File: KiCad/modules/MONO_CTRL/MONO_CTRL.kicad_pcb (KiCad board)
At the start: 4 copper layers, 15 x 14.8 mm, 50 parts, among them J1 Conn_01x01_Pin, J11 Conn_01x01_Pin, J12 Conn_01x01_Pin, J13 Conn_01x01_Pin, J14 Conn_01x01_Pin, J15 Conn_01x01_Pin, J16 Conn_01x01_Pin, J17 Conn_01x01_Pin, J18 Conn_01x01_Pin, J19 Conn_01x01_Pin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

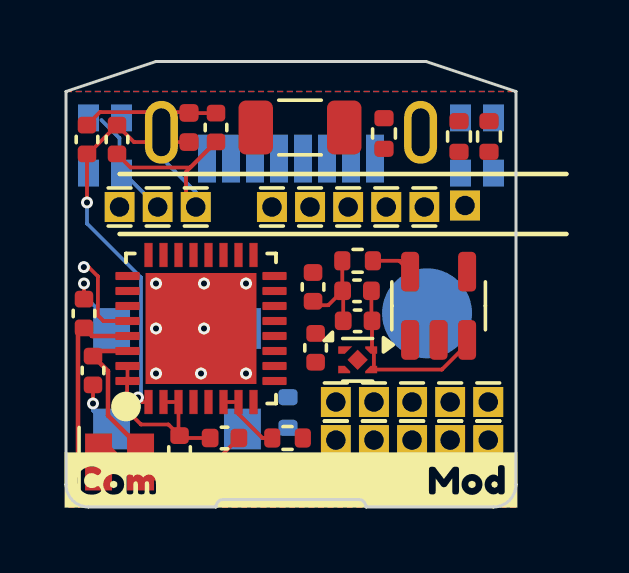
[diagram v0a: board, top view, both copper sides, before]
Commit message: finished mono moudule, should be ready for manufacture
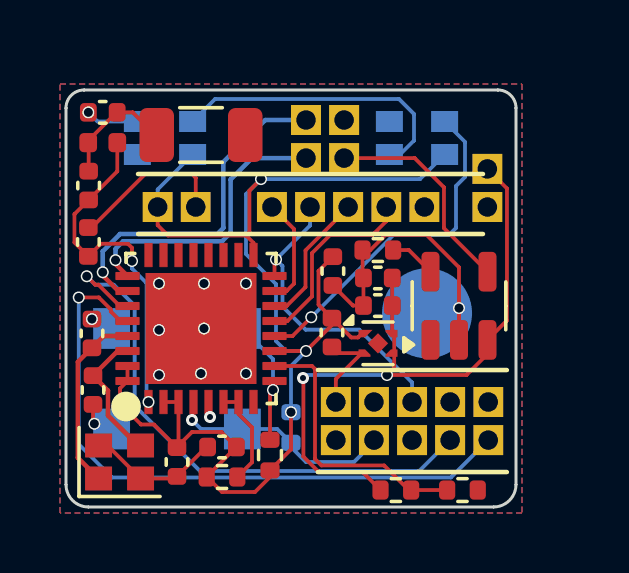
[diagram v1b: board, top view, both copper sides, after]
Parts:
- removed J19: Conn_01x01_Pin, Connector_PinHeader_1.27mm:PinHeader_1x01_P1.27mm_Vertical
- removed USB1: YTC-TC8S-125, 00_lcsc:USB-C-SMD_YIYUAN_YTC-TC8S-125
- removed kibuzzard-658C3FF8: G***, kibuzzard-658C3FF8
- added J10: Conn_01x01_Pin, Connector_PinHeader_1.27mm:PinHeader_1x01_P1.27mm_Vertical, F.Cu at (30.3, 24.1)
- added J23: Conn_01x01_Pin, Connector_PinHeader_1.27mm:PinHeader_1x01_P1.27mm_Vertical, F.Cu at (30.3, 25.4)
- added J25: Conn_01x01_Pin, Connector_PinHeader_1.27mm:PinHeader_1x01_P1.27mm_Vertical, F.Cu at (36.4, 27.0)
- added J26: Conn_01x01_Pin, Connector_PinHeader_1.27mm:PinHeader_1x01_P1.27mm_Vertical, F.Cu at (31.6, 24.1)
- added J4: Conn_01x01_Pin, Connector_PinHeader_1.27mm:PinHeader_1x01_P1.27mm_Vertical, F.Cu at (31.6, 25.4)
- added kibuzzard-66D6133A: G***, kibuzzard-66D6133A, B.Cu at (34.0, 36.3)
- moved R3 12.2 mm to (33.3, 36.5), turned to 180 degrees
- moved R6 11.8 mm to (35.5, 36.5), turned to 0 degrees
- moved R4 11.4 mm to (29.1, 35.3), turned to 90 degrees
- moved C1 3.81 mm to (23.5, 23.9), turned to 180 degrees
- moved C3 3.55 mm to (23.1, 28.2), turned to 90 degrees
- moved AE1 3.31 mm to (26.8, 24.6)
- moved L1 2.92 mm to (23.5, 24.9), turned to 0 degrees
- moved R5 2.54 mm to (27.5, 36.0), turned to 180 degrees
- moved LED1 2.02 mm to (25.6, 24.7), turned to 0 degrees
- moved LED2 2.02 mm to (34.0, 24.7), turned to 0 degrees
- moved C12 1.54 mm to (23.1, 26.3)
- moved J24 1.43 mm to (36.4, 25.8), turned to 180 degrees
- moved U3 0.87 mm to (32.7, 31.6)
- moved C10 0.85 mm to (31.2, 29.2)
- moved C8 0.85 mm to (32.7, 30.3)
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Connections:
- net /SPICS_ARM renamed /SPICS
- J11 pad 1: /IO1_out -> +3.3V
- J12 pad 1: /SWDIO/POCI_ARM -> /GPIO9
- J13 pad 1: /PICO_ARM -> /PICO
- J14 pad 1: /SCLK_ARM -> /GPIO8
- J16 pad 1: /i2C_SCL -> /U0RX
- J17 pad 1: /I2C_SDA -> /U0TX
- J18 pad 1: /AIN0 -> /PWM
- LED1 pad 1: Net-(LED1-DO) -> unconnected-(LED1-DO-Pad1)
- LED1 pad 3: /LED_IN -> Net-(LED1-DI)
- LED2 pad 1: /LED_OUT -> Net-(LED1-DI)
- LED2 pad 3: Net-(LED1-DO) -> /LED_IN
- U2 pad 4: /DIR -> /GPIO
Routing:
- net +3.3V: track 9.95 -> 56.4 mm, vias 0 -> 3
- net /U0RX: track 0.00 -> 19.0 mm, vias 0 -> 1
- net /U0TX: track 2.96 -> 21.5 mm
- net /GPIO9: track 0.00 -> 16.8 mm
- net +BATT: track 6.26 -> 22.2 mm, vias 0 -> 2
- net /USB_D+: track 0.00 -> 11.7 mm, vias 0 -> 1
- net /LED_IN: track 0.00 -> 11.5 mm, vias 0 -> 1
- net /GPIO8: track 0.00 -> 11.4 mm
- net /PICO: track 0.00 -> 10.5 mm, vias 0 -> 1
- net Net-(LED1-DI): track 0.00 -> 9.80 mm
- net /USB_D-: track 0.00 -> 9.71 mm, vias 0 -> 1
- net /ADC_BATT: track 0.00 -> 9.23 mm
- net /GPIO: track 0.00 -> 7.69 mm, vias 0 -> 1
- net +5V: track 0.00 -> 7.14 mm
- net /CSB: track 0.00 -> 6.42 mm
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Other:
- board size 15 x 14.8 mm -> 15 x 13.9 mm
- board text removed: "(SPI, I2C)"

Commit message: fixed MONOCOM ERC and DRC: via size, missing pins
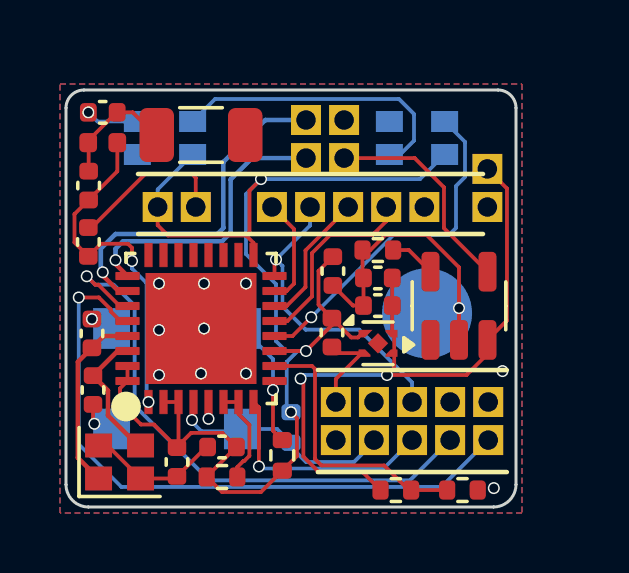
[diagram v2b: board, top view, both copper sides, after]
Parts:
- moved R4 0.41 mm to (29.5, 35.3)
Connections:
- U2 pad 8: /EN_DRV -> /SPICS
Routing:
- net /SPICS: track 0.00 -> 7.75 mm, vias 0 -> 1
- net +3.3V: track 56.4 -> 56.9 mm
- net GND: vias 12 -> 14
